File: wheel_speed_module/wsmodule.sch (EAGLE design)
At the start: 19 parts, among them T1 BC849, U1 LTC2875XS

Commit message: Version 1.1
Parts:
- added J1: J5MM, jumper:J5MM
- C1: value (none) -> 47u; device eagle-ltspice:C -> eagle-ltspice:CC1210
- R1, R2, R3, R4: device eagle-ltspice:R -> eagle-ltspice:RR1206
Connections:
- new net 3V3R: J1.2, R4.2
- net 3V3: now also J1.1; no longer R4.2
- net GND: now also JP2.12
- net VCC: no longer C2_VCC.P
- net VIN: now also C2_VCC.P
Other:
- moved on the sheet: C1, C1_CANH, C1_CANL, C1_GND, C1_VCC, C2_GND, C2_SIG, C2_VCC, D1, D2, F1, JP1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

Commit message: Version 1.2
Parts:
- removed D1: BZX84CSMD, diode:BZX84CSMD
- removed J1: J5MM, jumper:J5MM
- added C3: 100uF, rcl:CPOL-EUD
- added C4: 10uF, rcl:CPOL-EUC
- added IC1: 7805DT, linear:7805DT
- renumbered C1_CANH to CANH, C1_CANL to CANL, C1_GND to GND, C1_VCC to VCC, C2_GND to SGND, C2_SIG to SIG, C2_VCC to SVCC
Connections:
- removed net 3V3R: J1.2, R4.2
- new net N$2: C4.+, IC1.VO, JP2.1
- net 3V3: now also R4.2; no longer J1.1
- net GND: now also C3.-, C4.-, IC1.GND; no longer D1.A
- net VIN: now also C3.+, IC1.VI; no longer D1.C, JP2.1
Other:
- note added: "https://www.reichelt.de/Electrolyte-Capacitors-SMD-Low-ESR-105-C/EEHZA-100U-25/3/index.html?ACTION=3&LA=2&ARTICLE=200188&GROUPID=4001&artnr=EEHZA+100U+25&SEARCH=%252A"
- note added: "https://www.reichelt.de/Electrolyte-Capacitors-SMD-Low-ESR-105-C/EEHZA-10U-50/3/index.html?ACTION=3&LA=2&ARTICLE=200178&GROUPID=4001&artnr=EEHZA+10U+50&SEARCH=%252A"
- moved on the sheet: F1, JP1, JP2

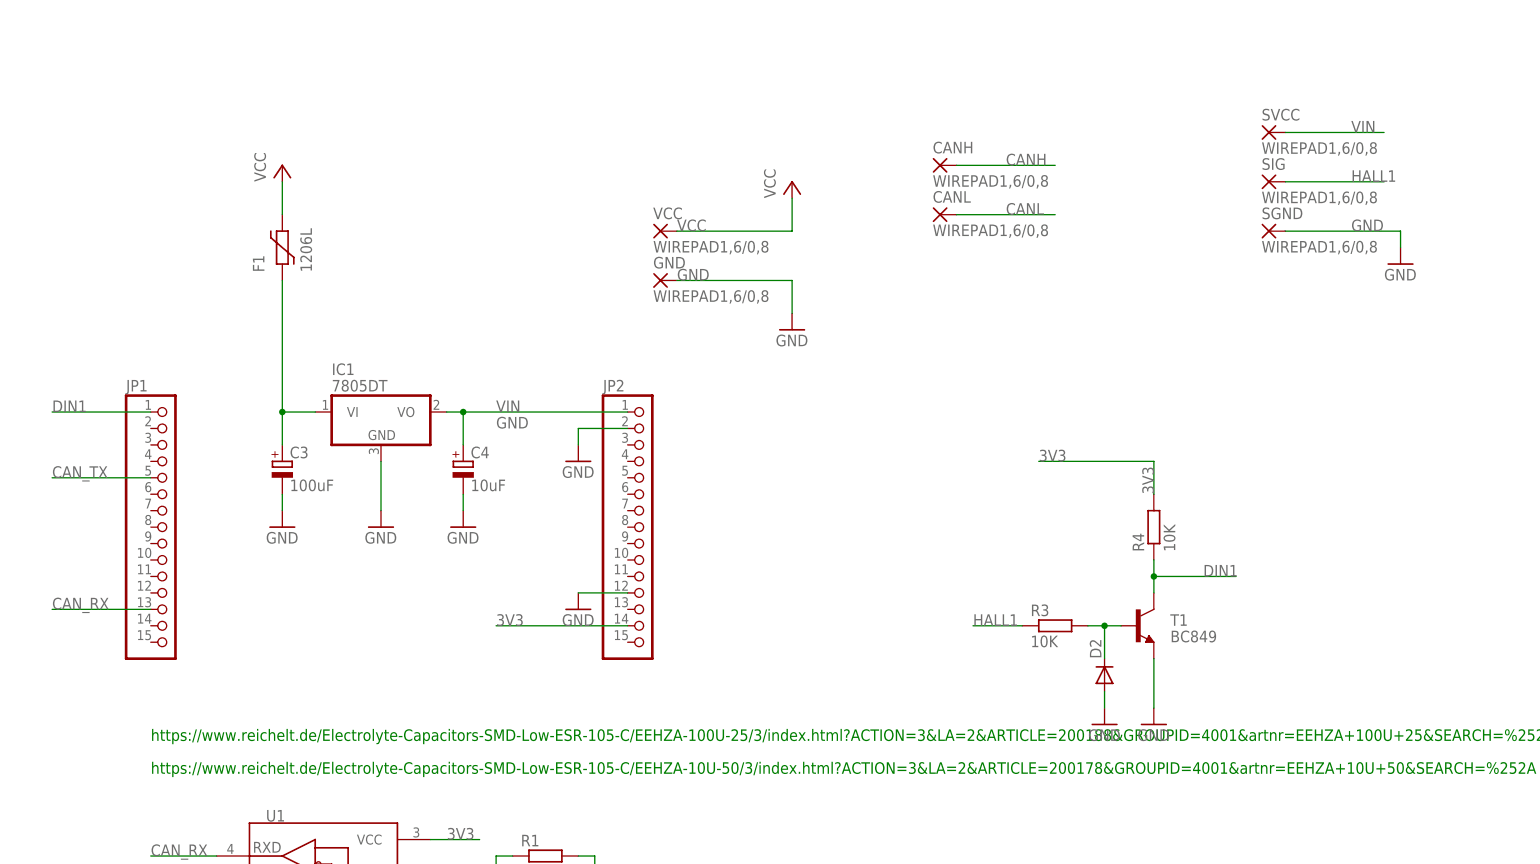
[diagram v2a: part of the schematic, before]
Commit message: Version 1.3
Two sided assembly. New M8 connectors at each end.
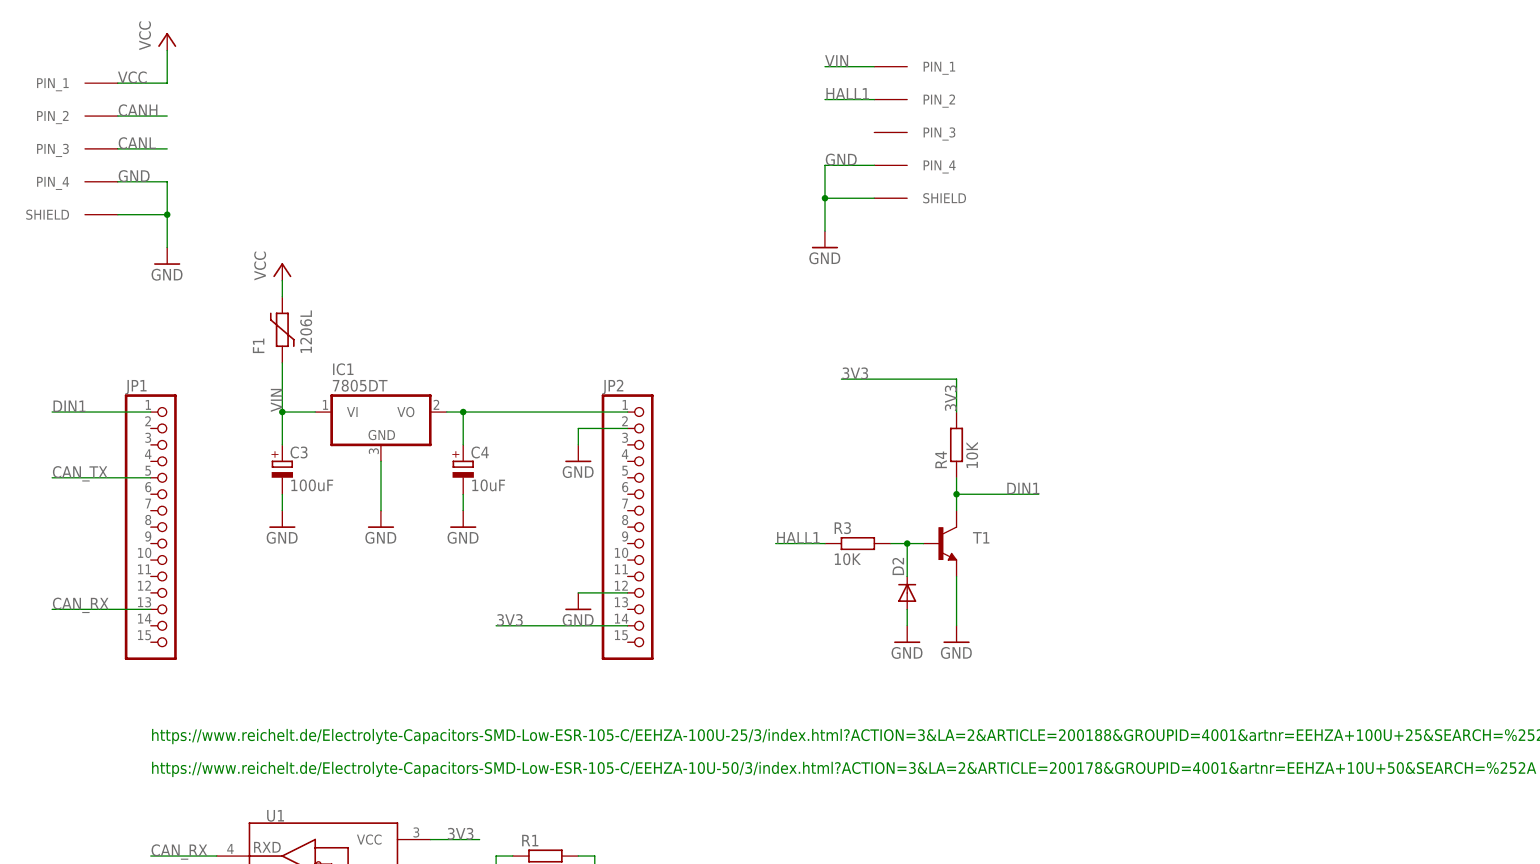
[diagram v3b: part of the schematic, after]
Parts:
- removed CANH, CANL, GND, SGND, SIG, SVCC, VCC: WIREPAD1,6/0,8, wirepad:WIREPAD1,6/0,8
- added INPUT: M8-718-MALE, SamacSys_Parts:M8-718-MALE
- added OUTPUT: M8-718-FEMALE, SamacSys_Parts:M8-718-FEMALE
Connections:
- net N$2 renamed 5V
- net CANH: now also INPUT.PIN_2; no longer CANH.P
- net CANL: now also INPUT.PIN_3; no longer CANL.P
- net GND: now also INPUT.PIN_4, INPUT.SHIELD, OUTPUT.PIN_4, OUTPUT.SHIELD; no longer GND.P, SGND.P
- net HALL1: now also OUTPUT.PIN_2; no longer SIG.P
- net VCC: now also INPUT.PIN_1; no longer VCC.P
- net VIN: now also OUTPUT.PIN_1; no longer SVCC.P
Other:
- moved on the sheet: D2, F1, R3, R4, T1
